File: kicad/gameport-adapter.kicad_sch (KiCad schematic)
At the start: 7 parts

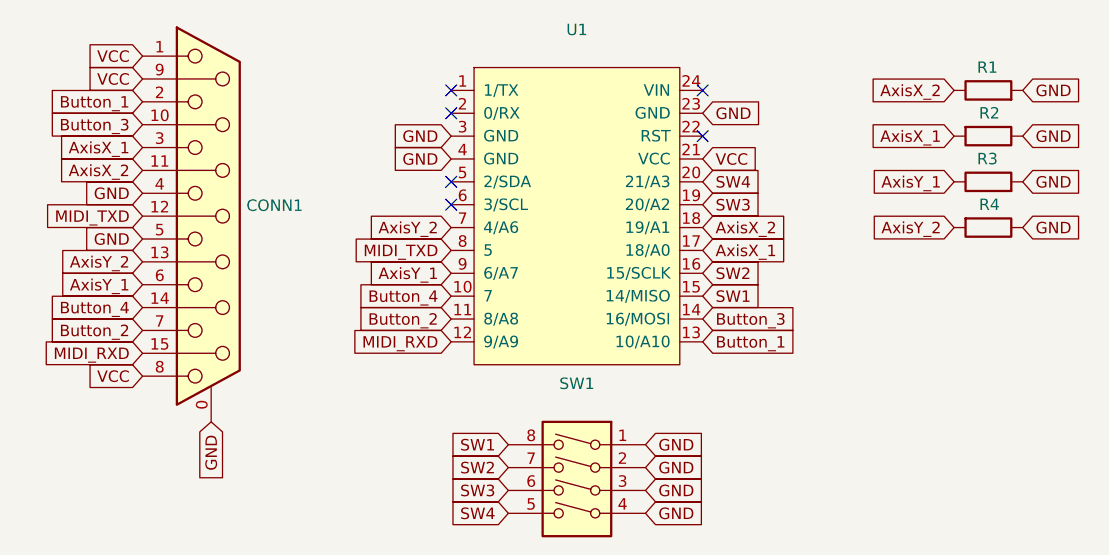
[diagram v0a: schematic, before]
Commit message: Change the powersupply of the gameport to VIN/RAW rather than VCC
In my case with the Sidewinder 3D Pro the joystick did not seem
to run stable. Maybe there was too much power drawn from VCC?
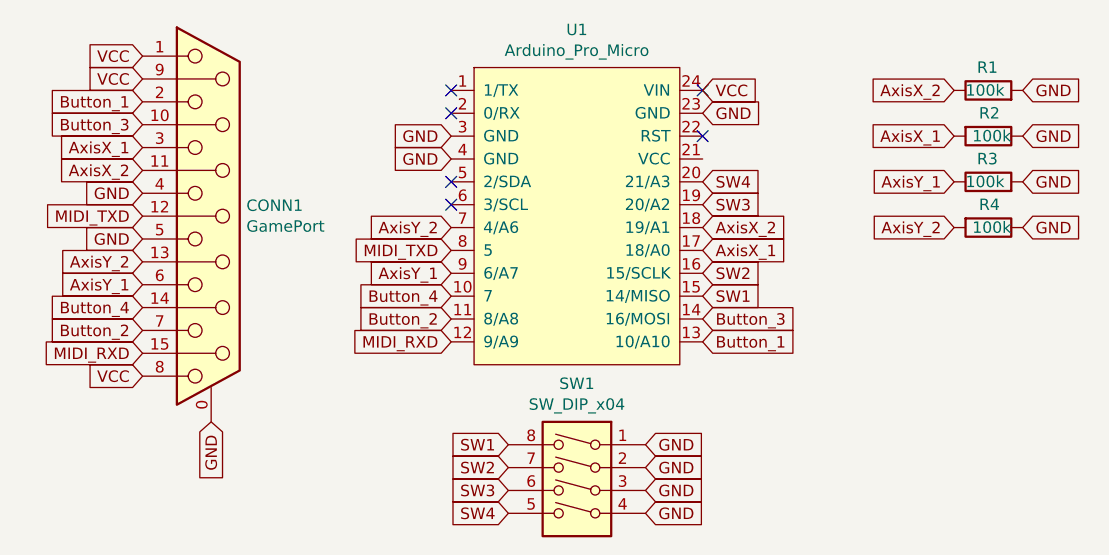
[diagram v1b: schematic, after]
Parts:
- CONN1: value (none) -> GamePort; footprint (none) -> Connector_Dsub:DSUB-15_Female_Horizontal_P2.77x2.84mm_EdgePinOffset7.70mm_Housed_MountingHolesOffset9.12mm
- R1, R2, R3, R4: value (none) -> 100k; footprint (none) -> Resistor_THT:R_Axial_DIN0204_L3.6mm_D1.6mm_P7.62mm_Horizontal
- SW1: value (none) -> SW_DIP_x04; footprint (none) -> Button_Switch_THT:SW_DIP_SPSTx04_Slide_9.78x12.34mm_W7.62mm_P2.54mm
- U1: value (none) -> Arduino_Pro_Micro; footprint (none) -> Package_DIP:DIP-24_W15.24mm_Socket
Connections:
- net VCC: now also U1.24 (VIN); no longer U1.21 (VCC)
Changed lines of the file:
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@@
     )
   )
-  (global_label "VCC" (shape input) (at 106.68 48.26 0) (fields_autoplaced)
-    (effects (font (size 1.27 1.27)) (justify left))
-    (property "Intersheet References" "${INTERSHEET_REFS}" (id 0) (at 0 0 0)
+  (global_label "VCC" (shape input) (at 106.68 40.64 0) (fields_autoplaced)
+    (effects (font (size 1.27 1.27)) (justify left))
+    (property "Intersheet References" "${INTERSHEET_REFS}" (id 0) (at 0 -7.62 0)
       (effects (font (size 1.27 1.27)) hide)
     )
@@
       (effects (font (size 1.27 1.27)) (justify left))
     )
-    (property "Value" "" (id 1) (at 55.9816 55.753 0)
+    (property "Value" "GamePort" (id 1) (at 55.9816 55.753 0)
       (effects (font (size 1.27 1.27)) (justify left))
     )
-    (property "Footprint" "" (id 2) (at 52.07 54.61 0)
+    (property "Footprint" "Connector_Dsub:DSUB-15_Female_Horizontal_P2.77x2.84mm_EdgePinOffset7.70mm_Housed_MountingHolesOffset9.12mm" (id 2) (at 52.07 54.61 0)
       (effects (font (size 1.27 1.27)) hide)
     )
@@
     (in_bom yes) (on_board yes)
     (property "Reference" "U1" (id 0) (at 92.71 33.909 0))
-    (property "Value" "" (id 1) (at 92.71 36.2204 0))
-    (property "Footprint" "" (id 2) (at 78.74 35.56 0)
+    (property "Value" "Arduino_Pro_Micro" (id 1) (at 92.71 36.2204 0))
+    (property "Footprint" "Package_DIP:DIP-24_W15.24mm_Socket" (id 2) (at 78.74 35.56 0)
       (effects (font (size 1.27 1.27)) hide)
     )
@@
     (in_bom yes) (on_board yes)
     (property "Reference" "SW1" (id 0) (at 92.71 73.2282 0))
-    (property "Value" "" (id 1) (at 92.71 75.5396 0))
-    (property "Footprint" "" (id 2) (at 92.71 85.09 0)
+    (property "Value" "SW_DIP_x04" (id 1) (at 92.71 75.5396 0))
+    (property "Footprint" "Button_Switch_THT:SW_DIP_SPSTx04_Slide_9.78x12.34mm_W7.62mm_P2.54mm" (id 2) (at 92.71 85.09 0)
       (effects (font (size 1.27 1.27)) hide)
     )
@@
       (effects (font (size 1.27 1.27)) (justify right))
     )
-    (property "Value" "" (id 1) (at 135.89 40.64 90)
-      (effects (font (size 1.27 1.27)) (justify right))
-    )
-    (property "Footprint" "" (id 2) (at 138.43 42.418 90)
+    (property "Value" "100k" (id 1) (at 135.89 40.64 90)
+      (effects (font (size 1.27 1.27)) (justify right))
+    )
+    (property "Footprint" "Resistor_THT:R_Axial_DIN0204_L3.6mm_D1.6mm_P7.62mm_Horizontal" (id 2) (at 138.43 42.418 90)
       (effects (font (size 1.27 1.27)) hide)
     )
@@
       (effects (font (size 1.27 1.27)) (justify right))
     )
-    (property "Value" "" (id 1) (at 140.97 45.72 90)
-      (effects (font (size 1.27 1.27)) (justify right))
-    )
-    (property "Footprint" "" (id 2) (at 138.43 43.942 90)
+    (property "Value" "100k" (id 1) (at 140.97 45.72 90)
+      (effects (font (size 1.27 1.27)) (justify right))
+    )
+    (property "Footprint" "Resistor_THT:R_Axial_DIN0204_L3.6mm_D1.6mm_P7.62mm_Horizontal" (id 2) (at 138.43 43.942 90)
       (effects (font (size 1.27 1.27)) hide)
     )
@@
       (effects (font (size 1.27 1.27)) (justify right))
     )
-    (property "Value" "" (id 1) (at 135.89 50.8 90)
-      (effects (font (size 1.27 1.27)) (justify right))
-    )
-    (property "Footprint" "" (id 2) (at 138.43 52.578 90)
+    (property "Value" "100k" (id 1) (at 135.89 50.8 90)
+      (effects (font (size 1.27 1.27)) (justify right))
+    )
+    (property "Footprint" "Resistor_THT:R_Axial_DIN0204_L3.6mm_D1.6mm_P7.62mm_Horizontal" (id 2) (at 138.43 52.578 90)
       (effects (font (size 1.27 1.27)) hide)
     )
@@
       (effects (font (size 1.27 1.27)) (justify right))
     )
-    (property "Value" "" (id 1) (at 140.97 55.88 90)
-      (effects (font (size 1.27 1.27)) (justify right))
-    )
-    (property "Footprint" "" (id 2) (at 138.43 54.102 90)
-      (effects (font (size 1.27 1.27)) hide)
-    )
+    (property "Value" "100k" (id 1) (at 140.97 55.88 90)
+      (effects (font (size 1.27 1.27)) (justify right))
+    )
+    (property "Footprint" "Resistor_THT:R_Axial_DIN0204_L3.6mm_D1.6mm_P7.62mm_Horizontal" (id 2) (at 138.43 54.102 90)
+      (effects (font (size 1.27 1.27)) hide)
+    )
